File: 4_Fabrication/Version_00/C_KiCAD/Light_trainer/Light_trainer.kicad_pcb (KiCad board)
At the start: 2 copper layers, 47 parts, among them J1 USB_B_Micro, Q2 S8050, Q3 S8050, SW1 SW_Push, SW2 SW_Push, SW3 SW_Push, SW4 SW_Push, SW5 SW_Push, SW6 SW_DIP_x04, SW7 SW_Push, U1 ESP32-DevKitC-32D, U2 ESP32-WROOM-32, U3 LTC3525-5, U5 CP2104

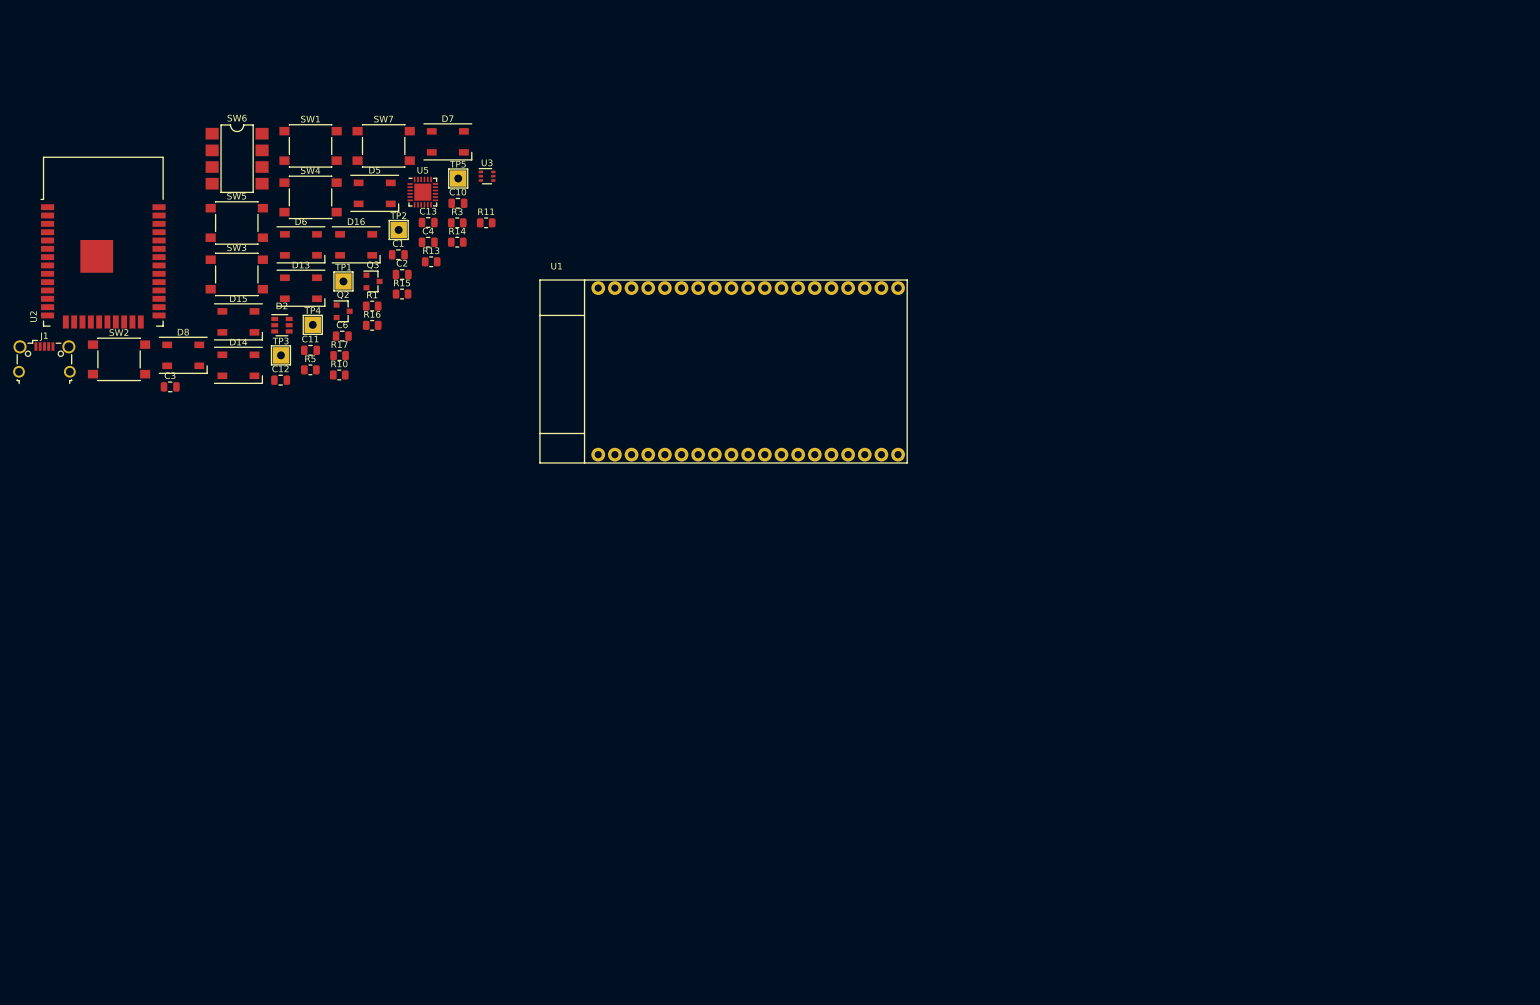
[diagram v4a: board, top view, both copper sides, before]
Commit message: ADD all footprint
All footprint
miss 1 3d (battery holder 3xAA)
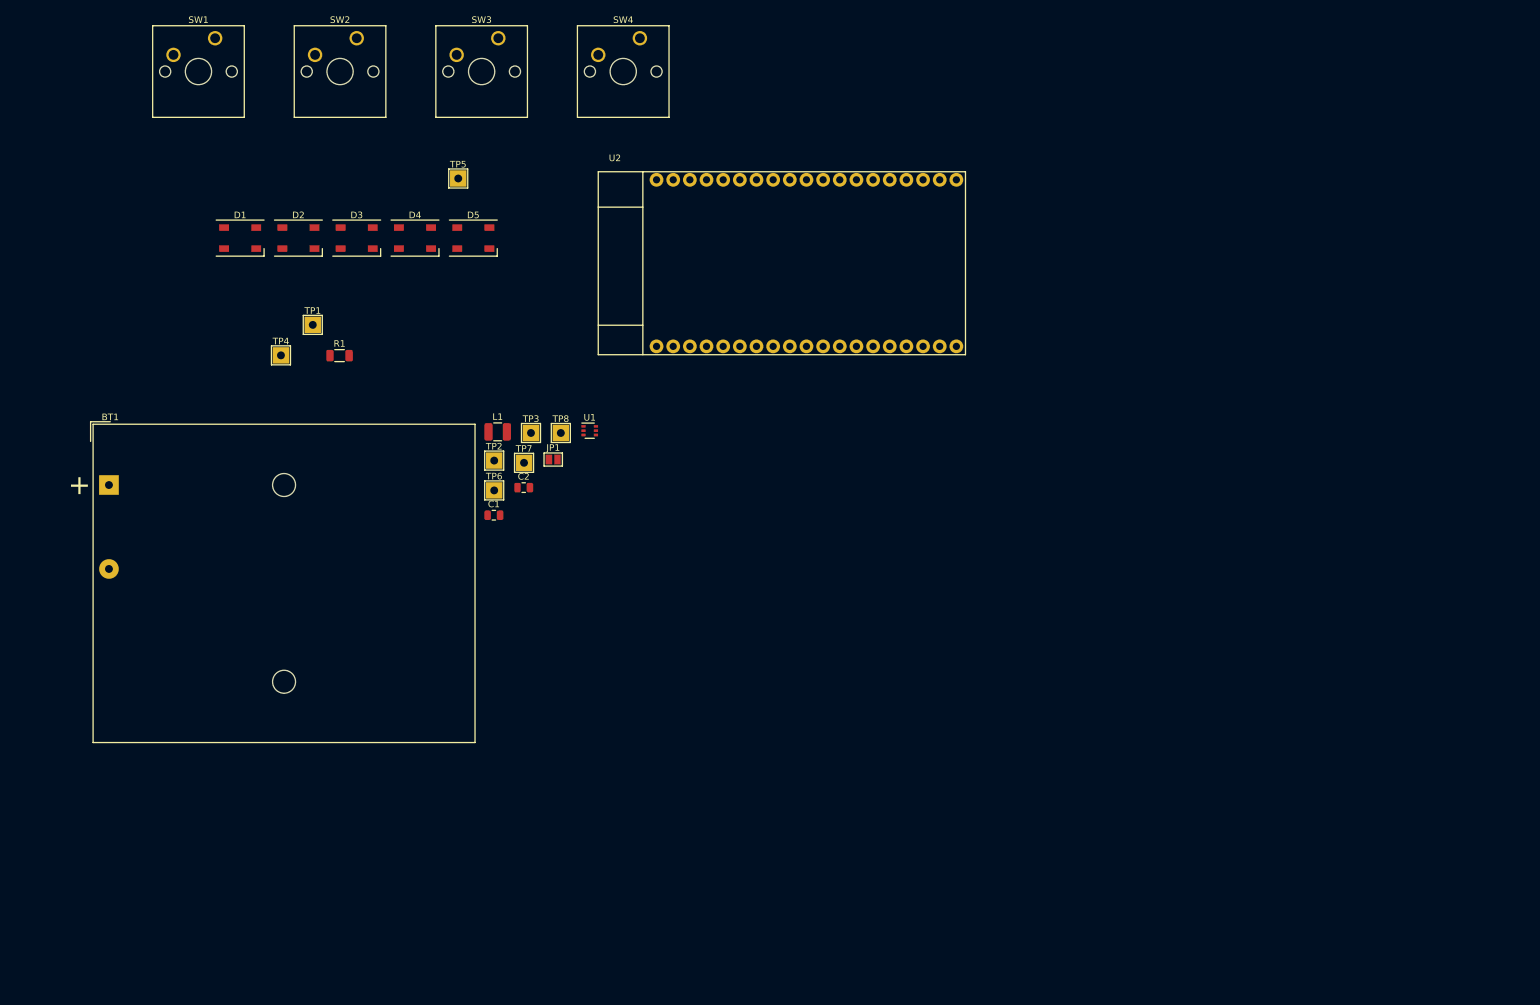
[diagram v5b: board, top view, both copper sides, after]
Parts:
- removed C10, C3: 10uF, Capacitor_SMD:C_0805_2012Metric
- removed C11, C13: 0,1uF, Capacitor_SMD:C_0805_2012Metric
- removed C12, C6: 1uF, Capacitor_SMD:C_0805_2012Metric
- removed C4: 4,7uF, Capacitor_SMD:C_0805_2012Metric
- removed D13, D14, D15: SK6812, LED_SMD:LED_SK6812_PLCC4_5.0x5.0mm_P3.2mm
- removed the D2 at (81.3, 62.8)
- removed J1: USB_B_Micro, Connector_USB:USB_Micro-B_Wuerth_629105150521_CircularHoles
- removed Q2, Q3: S8050, Package_TO_SOT_SMD:SOT-23
- removed the R1 at (95.1, 59.9)
- removed R10, R11, R13, R14, R15, R16: 10K, Resistor_SMD:R_0805_2012Metric
- removed R3: 4k, Resistor_SMD:R_0805_2012Metric
- removed R5: 10k, Resistor_SMD:R_0805_2012Metric
- removed the SW2 at (56.5, 68.0)
- removed the SW3 at (74.4, 55.1)
- removed SW6: SW_DIP_x04, Package_DIP:SMDIP-8_W7.62mm
- removed the TP1 at (90.7, 56.1)
- removed the U2 at (54.1, 53.1)
- removed U3: LTC3525-5, Package_TO_SOT_SMD:SOT-363_SC-70-6
- removed U5: CP2104, Package_DFN_QFN:QFN-24-1EP_4x4mm_P0.5mm_EP2.6x2.6mm
- added BT1: Battery, Battery:BatteryHolder_TruPower_BH-331P_3xAA, F.Cu at (54.9, 87.2)
- added JP1: Jumper, Jumper:SolderJumper-2_P1.3mm_Open_Pad1.0x1.5mm, F.Cu at (122.7, 83.3)
- added L1: 10uH, Inductor_SMD:L_1210_3225Metric, F.Cu at (114.2, 79.1)
- added TP3: TestPoint, TestPoint:TestPoint_THTPad_2.5x2.5mm_Drill1.2mm, F.Cu at (119.3, 79.2)
- added TP6: TestPoint, TestPoint:TestPoint_THTPad_2.5x2.5mm_Drill1.2mm, F.Cu at (113.7, 88.0)
- added TP7: TestPoint, TestPoint:TestPoint_THTPad_2.5x2.5mm_Drill1.2mm, F.Cu at (118.2, 83.8)
- added TP8: TestPoint, TestPoint:TestPoint_THTPad_2.5x2.5mm_Drill1.2mm, F.Cu at (123.8, 79.2)
- added U1: LTC3525-5, Package_TO_SOT_SMD:SOT-363_SC-70-6, F.Cu at (128.2, 78.9)
- C1: value 22uF -> 1uF
- C2: value 0,1uF -> 10uF
- R1: renamed from R17; footprint Resistor_SMD:R_0805_2012Metric -> Resistor_SMD:R_1206_3216Metric
- SW1: footprint Button_Switch_SMD:SW_SPST_PTS645 -> Work_Forestier:SW_Cherry_MX_1.00u_PCB_3D
- SW2: renamed from SW4; footprint Button_Switch_SMD:SW_SPST_PTS645 -> Work_Forestier:SW_Cherry_MX_1.00u_PCB_3D
- SW3: renamed from SW5; footprint Button_Switch_SMD:SW_SPST_PTS645 -> Work_Forestier:SW_Cherry_MX_1.00u_PCB_3D
- SW4: renamed from SW7; footprint Button_Switch_SMD:SW_SPST_PTS645 -> Work_Forestier:SW_Cherry_MX_1.00u_PCB_3D
- moved SW3 48.8 mm to (114.3, 19.1)
- moved SW4 42.4 mm to (135.9, 19.1)
- moved C1 42.3 mm to (113.6, 91.8)
- moved D4 39.6 mm to (101.6, 49.5)
- moved TP2 38.1 mm to (113.7, 83.5)
- moved C2 37.4 mm to (118.2, 87.6)
- moved SW2 25.3 mm to (92.7, 19.1)
- moved SW1 21.9 mm to (71.1, 19.1)
- moved D1 21.6 mm to (74.9, 49.5)
- moved D3 20.2 mm to (92.7, 49.5)
- moved U2 18.8 mm to (129.5, 67.3)
- moved D5 17.9 mm to (110.5, 49.5)
- moved D2 1.09 mm to (83.8, 49.5)
- renumbered D5 to D1, D6 to D2, D7 to D3, D8 to D4, D16 to D5, TP4 to TP1, TP3 to TP4, U1 to U2
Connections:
- C1 pad 1: +3V3 -> Net-(C1-Pad1)
- C2 pad 1: +3V3 -> +5V
- D4 pad 4: DOUT -> Net-(D4-Pad4)
- D5 pad 2: Net-(D15-Pad4) -> Net-(D4-Pad4)
- SW1 pad 1: GND -> +3V3
- SW1 pad 2: IO0 -> switch
- TP2 pad 1: +5V -> Net-(C1-Pad1)
- U2 pad 3V3: Net-(U1-Pad3V3) -> +3V3
- U2 pad 5V: Net-(U1-Pad5V) -> +5V
- U2 pad CLK: Net-(U1-PadCLK) -> (no net)
- U2 pad CMD: Net-(U1-PadCMD) -> (no net)
- U2 pad EN: Net-(U1-PadEN) -> (no net)
- U2 pad GND0: Net-(U1-PadGND0) -> GND
- U2 pad GND1: Net-(U1-PadGND1) -> GND
- U2 pad GND2: Net-(U1-PadGND2) -> GND
- U2 pad IO0: Net-(U1-PadIO0) -> (no net)
- U2 pad IO12: Net-(U1-PadIO12) -> (no net)
- U2 pad IO13: Net-(U1-PadIO13) -> (no net)
- U2 pad IO14: Net-(U1-PadIO14) -> (no net)
- U2 pad IO15: Net-(U1-PadIO15) -> (no net)
- U2 pad IO16: Net-(U1-PadIO16) -> LED
- U2 pad IO17: Net-(U1-PadIO17) -> switch
- U2 pad IO18: Net-(U1-PadIO18) -> (no net)
- U2 pad IO19: Net-(U1-PadIO19) -> (no net)
- U2 pad IO2: Net-(U1-PadIO2) -> (no net)
- U2 pad IO21: Net-(U1-PadIO21) -> (no net)
- U2 pad IO22: Net-(U1-PadIO22) -> (no net)
- U2 pad IO23: Net-(U1-PadIO23) -> (no net)
- U2 pad IO25: Net-(U1-PadIO25) -> (no net)
- U2 pad IO26: Net-(U1-PadIO26) -> (no net)
- U2 pad IO27: Net-(U1-PadIO27) -> (no net)
- U2 pad IO32: Net-(U1-PadIO32) -> (no net)
- U2 pad IO33: Net-(U1-PadIO33) -> (no net)
- U2 pad IO34: Net-(U1-PadIO34) -> (no net)
- U2 pad IO35: Net-(U1-PadIO35) -> (no net)
- U2 pad IO4: Net-(U1-PadIO4) -> (no net)
- U2 pad IO5: Net-(U1-PadIO5) -> (no net)
- U2 pad RXD0: Net-(U1-PadRXD0) -> (no net)
- U2 pad SD0: Net-(U1-PadSD0) -> (no net)
- U2 pad SD1: Net-(U1-PadSD1) -> (no net)
- U2 pad SD2: Net-(U1-PadSD2) -> (no net)
- U2 pad SD3: Net-(U1-PadSD3) -> (no net)
- U2 pad SVN: Net-(U1-PadSVN) -> (no net)
- U2 pad SVP: Net-(U1-PadSVP) -> (no net)
- U2 pad TXD0: Net-(U1-PadTXD0) -> (no net)

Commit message: add all 3D
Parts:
- BT1: footprint Battery:BatteryHolder_TruPower_BH-331P_3xAA -> Work_Forestier:BatteryHolder_Keystone_2464_3xAA

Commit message: first routage
first placement + start routage
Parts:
- BT1: moved to B.Cu
- moved SW2 157.3 mm to (165.1, 158.8), turned to 180 degrees
- moved TP5 140.0 mm to (195.6, 149.9)
- moved SW3 138.3 mm to (214.6, 114.3), turned to 270 degrees
- moved D5 132.0 mm to (201.9, 144.8)
- moved D1 108.8 mm to (165.1, 110.5)
- moved D2 108.0 mm to (134.6, 144.8)
- moved D4 103.3 mm to (200.7, 78.7)
- moved SW1 102.9 mm to (120.7, 109.2), turned to 90 degrees
- moved U2 99.7 mm to (198.1, 139.7), turned to 90 degrees
- moved BT1 93.7 mm to (139.7, 127.0)
- moved TP1 91.0 mm to (167.6, 102.9)
- moved TP4 70.5 mm to (139.7, 106.7)
- moved R1 63.8 mm to (144.8, 100.3), turned to 270 degrees
- moved TP2 59.1 mm to (153.7, 127.0)
- moved SW4 57.2 mm to (170.2, 64.8)
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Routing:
- net +5V: track 0.00 -> 290.4 mm, vias 0 -> 2
- net GND: track 0.00 -> 277.5 mm
- net +3V3: track 0.00 -> 263.5 mm
- net switch: track 0.00 -> 244.2 mm, vias 0 -> 1
- net Net-(D2-Pad4): track 0.00 -> 97.5 mm, vias 0 -> 2
- net Net-(D3-Pad4): track 0.00 -> 84.9 mm
- net Net-(D4-Pad4): track 0.00 -> 65.5 mm
- net Net-(D1-Pad4): track 0.00 -> 55.7 mm
- net Net-(C1-Pad1): track 0.00 -> 29.3 mm
- net Net-(BT1-Pad1): track 0.00 -> 24.9 mm
- net LED: track 0.00 -> 9.87 mm
- net Net-(L1-Pad2): track 0.00 -> 7.85 mm
- net Net-(D5-Pad4): track 0.00 -> 6.58 mm
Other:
- board outline added: 105.2 x 105.2 mm

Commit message: placement + routage
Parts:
- added REF**: WEEE-Logo_5.6x8mm_SilkScreen, Symbol:WEEE-Logo_5.6x8mm_SilkScreen, F.Cu at (126.6, 61.2)
- added REF**: ESD-Logo_8.9x8mm_SilkScreen, Symbol:ESD-Logo_8.9x8mm_SilkScreen, F.Cu at (117.5, 61.3)
- added SW5: SW_SPDT, Work_Forestier:C&K-1101M2S5CQE2, B.Cu at (100.3, 74.9)
- moved TP4 42.3 mm to (111.8, 74.9)
- moved BT1 33.8 mm to (111.8, 108.0)
- moved TP5 30.2 mm to (167.6, 138.4)
- moved C1 30.2 mm to (118.1, 99.1)
- moved L1 30.2 mm to (121.9, 94.0)
- moved SW1 30.2 mm to (92.7, 97.8)
- moved U1 30.2 mm to (121.9, 99.1)
- moved D2 30.2 mm to (106.7, 133.3)
- moved D5 30.2 mm to (174.0, 133.3)
- moved SW2 30.2 mm to (137.2, 147.3)
- moved TP1 30.2 mm to (139.7, 91.4)
- moved TP3 30.2 mm to (120.7, 115.6)
- moved C2 30.2 mm to (127.0, 99.1)
- moved D1 30.2 mm to (137.2, 99.1)
- moved D3 30.2 mm to (106.7, 67.3)
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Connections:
- JP1 pad 1: Net-(BT1-Pad1) -> Net-(JP1-Pad1)
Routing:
- net Net-(JP1-Pad1): track 0.00 -> 29.8 mm, vias 0 -> 1
- net switch: track 244.2 -> 259.9 mm, vias 1 -> 2
- net Net-(BT1-Pad1): track 24.9 -> 34.3 mm, vias 0 -> 1
- net Net-(C1-Pad1): track 29.3 -> 37.4 mm, vias 0 -> 3
- net +5V: track 290.4 -> 285.3 mm
- net Net-(D2-Pad4): track 97.5 -> 94.2 mm
- net +3V3: track 263.5 -> 266.0 mm, vias 0 -> 1
- net Net-(D1-Pad4): track 55.7 -> 54.1 mm
- net Net-(D3-Pad4): track 84.9 -> 86.2 mm
- net GND: track 277.5 -> 277.3 mm, vias 0 -> 136
- added copper zone on B.Cu, net GND
- added copper zone on F.Cu, net GND
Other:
- board size 105.2 x 105.2 mm -> 110 x 110 mm
- board text added: "AA"
- board text added: "Bottom"
- board text added: "ON - OFF"
- board text added: "Top"
- board text added: "©Robin Forestier | 2021 Light Trainer V1"
